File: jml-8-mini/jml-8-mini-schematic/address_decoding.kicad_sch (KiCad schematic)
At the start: 3 parts, among them U6 74LS04, U8 74LS139, U9 74LS32

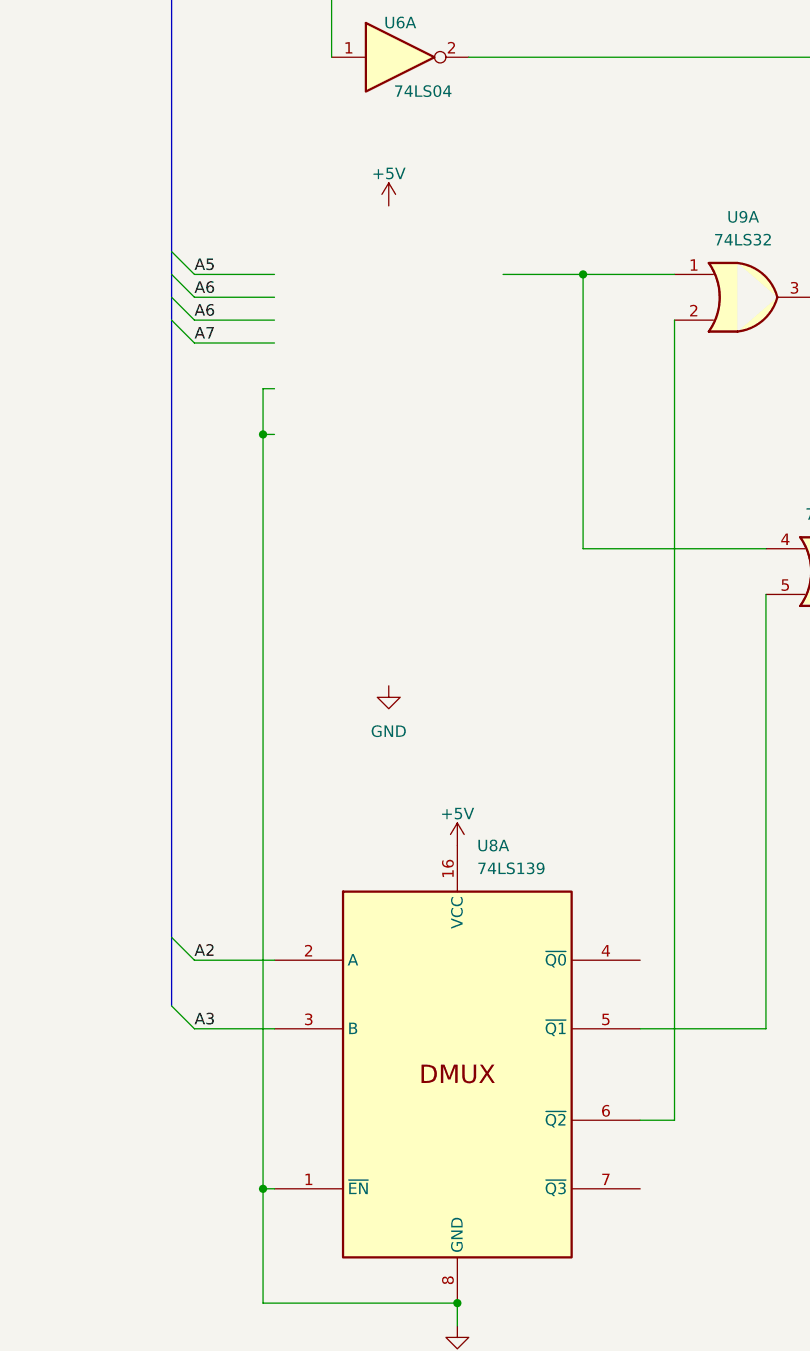
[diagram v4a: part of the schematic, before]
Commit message: lots of changes to schematic, redone to make easier to read and add to
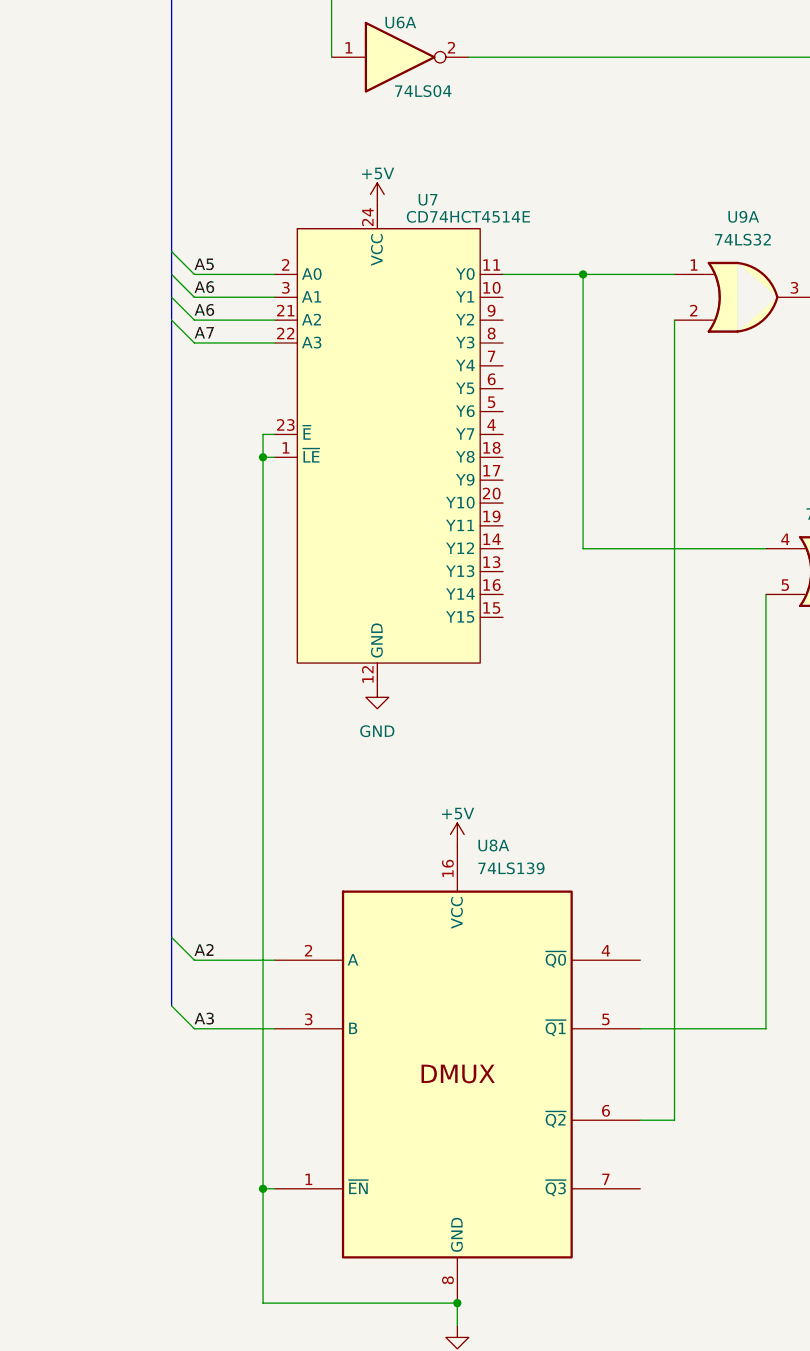
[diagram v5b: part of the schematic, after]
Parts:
- added U7: CD74HCT4514E, symbol jml-8-mini-library:CD74HCT4514E
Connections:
- net +5V: now also U7.24 (VCC)
- net A5: now also U7.2 (A0)
- net A6: now also U7.21 (A2), U7.3 (A1)
- net A7: now also U7.22 (A3)
- net GND: now also U7.1 (~{LE}), U7.12 (GND), U7.23 (~{E})
- net at U9.1, U9.4: now also U7.11 (Y0)
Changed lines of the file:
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@@
   (junction (at 85.09 185.42) (diameter 0) (color 0 0 0 0)
   )
+  (junction (at 63.5 91.44) (diameter 0) (color 0 0 0 0)
+  )
   (junction (at 63.5 172.72) (diameter 0) (color 0 0 0 0)
   )
-  (junction (at 63.5 88.9) (diameter 0) (color 0 0 0 0)
-  )
   (junction (at 53.34 29.21) (diameter 0) (color 0 0 0 0)
   )
@@
     (stroke (width 0) (type default))
   )
+  (wire (pts (xy 63.5 91.44) (xy 64.77 91.44))
+    (stroke (width 0) (type default))
+  )
   (bus (pts (xy 53.34 73.66) (xy 53.34 76.2))
     (stroke (width 0) (type default))
@@
     (stroke (width 0) (type default))
   )
-  (wire (pts (xy 63.5 88.9) (xy 63.5 172.72))
+  (wire (pts (xy 63.5 88.9) (xy 63.5 91.44))
     (stroke (width 0) (type default))
   )
@@
     (stroke (width 0) (type default))
   )
-  (wire (pts (xy 64.77 83.82) (xy 63.5 83.82))
-    (stroke (width 0) (type default))
-  )
   (wire (pts (xy 134.62 104.14) (xy 143.51 104.14))
     (stroke (width 0) (type default))
@@
     (stroke (width 0) (type default))
   )
-  (wire (pts (xy 63.5 83.82) (xy 63.5 88.9))
-    (stroke (width 0) (type default))
-  )
   (wire (pts (xy 55.88 154.94) (xy 64.77 154.94))
     (stroke (width 0) (type default))
@@
   )
   (wire (pts (xy 109.22 76.2) (xy 109.22 165.1))
+    (stroke (width 0) (type default))
+  )
+  (wire (pts (xy 63.5 91.44) (xy 63.5 172.72))
     (stroke (width 0) (type default))
   )
@@
         )
         (path "/7f93abb4-2372-4a9e-a664-5edb67349db4/0d9b5471-55ed-4c8b-801f-ea410459ca65"
-          (reference "#PWR?") (unit 1)
+          (reference "#PWR014") (unit 1)
         )
       )
@@
     )
   )
-  (symbol (lib_id "power:+5V") (at 77.47 63.5 0) (unit 1)
-    (in_bom yes) (on_board yes) (dnp no) (fields_autoplaced)
-    (property "Reference" "#PWR?" (at 77.47 67.31 0)
-      (effects (font (size 1.27 1.27)) hide)
-    )
-    (property "Value" "+5V" (at 77.47 59.944 0)
-      (effects (font (size 1.27 1.27)))
-    )
-    (property "Footprint" "" (at 77.47 63.5 0)
-      (effects (font (size 1.27 1.27)) hide)
-    )
-    (property "Datasheet" "" (at 77.47 63.5 0)
-      (effects (font (size 1.27 1.27)) hide)
-    )
-    (pin "1")
-    (instances
-      (project "jml-8-mini"
-        (path "/7f93abb4-2372-4a9e-a664-5edb67349db4/0d9b5471-55ed-4c8b-801f-ea410459ca65"
-          (reference "#PWR?") (unit 1)
+  (symbol (lib_id "power:+5V") (at 76.2 63.5 0) (unit 1)
+    (in_bom yes) (on_board yes) (dnp no) (fields_autoplaced)
+    (property "Reference" "#PWR06" (at 76.2 67.31 0)
+      (effects (font (size 1.27 1.27)) hide)
+    )
+    (property "Value" "+5V" (at 76.2 59.944 0)
+      (effects (font (size 1.27 1.27)))
+    )
+    (property "Footprint" "" (at 76.2 63.5 0)
+      (effects (font (size 1.27 1.27)) hide)
+    )
+    (property "Datasheet" "" (at 76.2 63.5 0)
+      (effects (font (size 1.27 1.27)) hide)
+    )
+    (pin "1")
+    (instances
+      (project "jml-8-mini"
+        (path "/7f93abb4-2372-4a9e-a664-5edb67349db4/0d9b5471-55ed-4c8b-801f-ea410459ca65"
+          (reference "#PWR06") (unit 1)
         )
       )
@@
     )
   )
-  (symbol (lib_id "power:GND") (at 77.47 116.84 0) (unit 1)
-    (in_bom yes) (on_board yes) (dnp no) (fields_autoplaced)
-    (property "Reference" "#PWR019" (at 77.47 123.19 0)
-      (effects (font (size 1.27 1.27)) hide)
-    )
-    (property "Value" "GND" (at 77.47 121.92 0)
-      (effects (font (size 1.27 1.27)))
-    )
-    (property "Footprint" "" (at 77.47 116.84 0)
-      (effects (font (size 1.27 1.27)) hide)
-    )
-    (property "Datasheet" "" (at 77.47 116.84 0)
+  (symbol (lib_id "jml-8-mini-library:CD74HCT4514E") (at 77.47 90.17 0) (unit 1)
+    (in_bom yes) (on_board yes) (dnp no)
+    (property "Reference" "U7" (at 80.645 62.865 0)
+      (effects (font (size 1.27 1.27)) (justify left))
+    )
+    (property "Value" "CD74HCT4514E" (at 79.375 64.77 0)
+      (effects (font (size 1.27 1.27)) (justify left))
+    )
+    (property "Footprint" "" (at 21.59 85.09 0)
+      (effects (font (size 1.27 1.27)) hide)
+    )
+    (property "Datasheet" "" (at 21.59 85.09 0)
+      (effects (font (size 1.27 1.27)) hide)
+    )
+    (pin "1")
+    (pin "10")
+    (pin "11")
+    (pin "12")
+    (pin "13")
+    (pin "14")
+    (pin "15")
+    (pin "16")
+    (pin "17")
+    (pin "18")
+    (pin "19")
+    (pin "2")
+    (pin "20")
+    (pin "21")
+    (pin "22")
+    (pin "23")
+    (pin "24")
+    (pin "3")
+    (pin "4")
+    (pin "5")
+    (pin "6")
+    (pin "7")
+    (pin "8")
+    (pin "9")
+    (instances
+      (project "jml-8-mini"
+        (path "/7f93abb4-2372-4a9e-a664-5edb67349db4/0d9b5471-55ed-4c8b-801f-ea410459ca65"
+          (reference "U7") (unit 1)
+        )
+      )
+    )
+  )
+  (symbol (lib_id "power:GND") (at 76.2 116.84 0) (unit 1)
+    (in_bom yes) (on_board yes) (dnp no) (fields_autoplaced)
+    (property "Reference" "#PWR019" (at 76.2 123.19 0)
+      (effects (font (size 1.27 1.27)) hide)
+    )
+    (property "Value" "GND" (at 76.2 121.92 0)
+      (effects (font (size 1.27 1.27)))
+    )
+    (property "Footprint" "" (at 76.2 116.84 0)
+      (effects (font (size 1.27 1.27)) hide)
+    )
+    (property "Datasheet" "" (at 76.2 116.84 0)
       (effects (font (size 1.27 1.27)) hide)
     )
@@
   (symbol (lib_id "power:+5V") (at 85.09 134.62 0) (unit 1)
     (in_bom yes) (on_board yes) (dnp no) (fields_autoplaced)
-    (property "Reference" "#PWR?" (at 85.09 138.43 0)
+    (property "Reference" "#PWR013" (at 85.09 138.43 0)
       (effects (font (size 1.27 1.27)) hide)
     )
@@
       (project "jml-8-mini"
         (path "/7f93abb4-2372-4a9e-a664-5edb67349db4/0d9b5471-55ed-4c8b-801f-ea410459ca65"
-          (reference "#PWR?") (unit 1)
-        )
-      )
+          (reference "#PWR013") (unit 1)
+        )
+      )

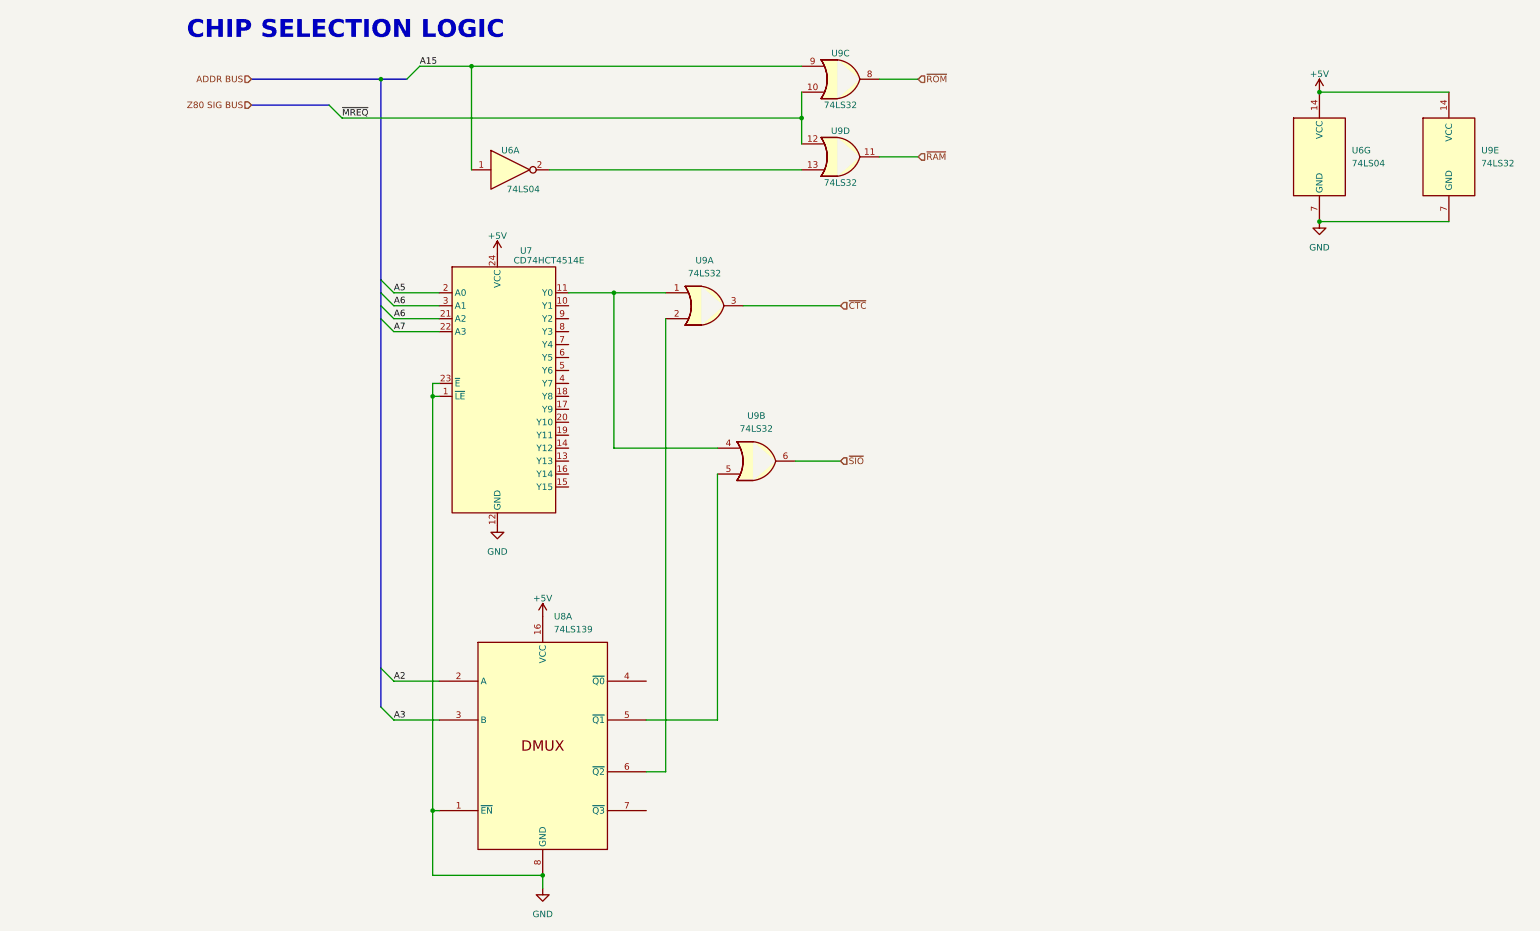
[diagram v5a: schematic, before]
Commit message: complete schematic
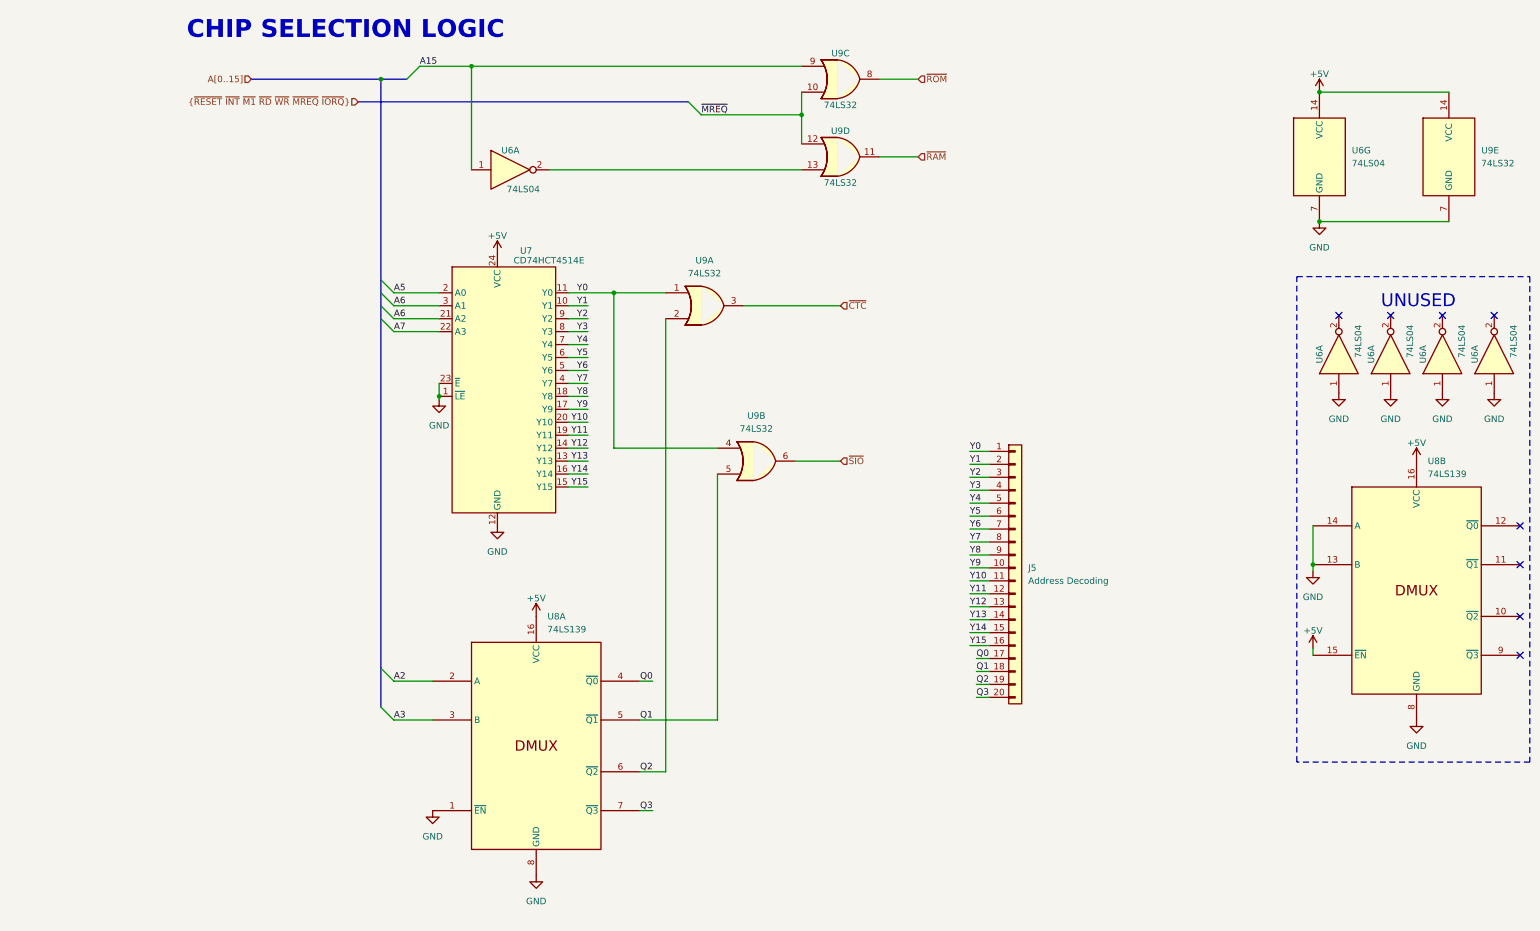
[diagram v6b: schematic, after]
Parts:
- added J5: Address Decoding, Connector_PinHeader_2.54mm:PinHeader_1x20_P2.54mm_Vertical, symbol Connector_Generic:Conn_01x20
- added U6 (x4): 74LS04, Package_DIP:DIP-14_W7.62mm_LongPads, symbol 74xx:74LS04
- added unit 2 of U8
- U6, U9: footprint (none) -> Package_DIP:DIP-14_W7.62mm_LongPads
- U7: footprint (none) -> Package_DIP:DIP-24_W15.24mm_LongPads
- U8: footprint (none) -> Package_DIP:DIP-16_W7.62mm_LongPads
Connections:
- net +5V: now also U8.15 (~{EN}), U8.16 (VCC)
- net GND: now also U6.1, U6.1, U6.1, U6.1, U8.13 (B), U8.14 (A), U8.8 (GND)
- net Y0: now reaches U7.11 (Y0), U9.1, U9.4
- net Y0: now also J5.1 (Pin_1)
- net Q2: now reaches U8.6 (~{Q2}), U9.2
- net Q2: now also J5.19 (Pin_19)
- net Q1: now reaches U8.5 (~{Q1}), U9.5
- net Q1: now also J5.18 (Pin_18)
- net Y1: now reaches U7.10 (Y1)
- net Y1: now also J5.2 (Pin_2)
- net Y13: now reaches U7.13 (Y13)
- net Y13: now also J5.14 (Pin_14)
- net Y12: now reaches U7.14 (Y12)
- net Y12: now also J5.13 (Pin_13)
- net Y15: now reaches U7.15 (Y15)
- net Y15: now also J5.16 (Pin_16)
- net Y14: now reaches U7.16 (Y14)
- net Y14: now also J5.15 (Pin_15)
- net Y9: now reaches U7.17 (Y9)
- net Y9: now also J5.10 (Pin_10)
- net Y8: now reaches U7.18 (Y8)
- net Y8: now also J5.9 (Pin_9)
- net Y11: now reaches U7.19 (Y11)
- net Y11: now also J5.12 (Pin_12)
- net Y10: now reaches U7.20 (Y10)
- net Y10: now also J5.11 (Pin_11)
- net Y7: now reaches U7.4 (Y7)
- net Y7: now also J5.8 (Pin_8)
- net Y6: now reaches U7.5 (Y6)
- net Y6: now also J5.7 (Pin_7)
- net Y5: now reaches U7.6 (Y5)
- net Y5: now also J5.6 (Pin_6)
- net Y4: now reaches U7.7 (Y4)
- net Y4: now also J5.5 (Pin_5)
- net Y3: now reaches U7.8 (Y3)
- net Y3: now also J5.4 (Pin_4)
- net Y2: now reaches U7.9 (Y2)
- net Y2: now also J5.3 (Pin_3)
- net Q0: now reaches U8.4 (~{Q0})
- net Q0: now also J5.17 (Pin_17)
- net Q3: now reaches U8.7 (~{Q3})
- net Q3: now also J5.20 (Pin_20)
- no-connect marks 0 -> 8
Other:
- note added: "UNUSED"
- moved on the sheet: U8A

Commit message: add to info section of schematic
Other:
- company: (none) -> https://github.com/jac-oblong/jml
- title: (none) -> JML-8 Mini Schematic
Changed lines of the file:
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@@
   (paper "A4")
   (title_block
+    (title "JML-8 Mini Schematic")
     (date "2023-10-02")
     (rev "A")
-    (comment 1 "Author: Jacob Long")
+    (company "https://github.com/jac-oblong/jml")
+    (comment 1 "Design of Z80 based microcomputer")
+    (comment 3 "Released under MIT License")
+    (comment 4 "Created by: Jacob Long (https://github.com/jac-oblong)")
   )
   (junction (at 237.49 57.15) (diameter 0) (color 0 0 0 0)

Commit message: update info section of schematic
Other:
- company: https://github.com/jac-oblong/jml -> https://github.com/jac-oblong/JML
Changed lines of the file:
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@@
     (date "2023-10-02")
     (rev "A")
-    (company "https://github.com/jac-oblong/jml")
+    (company "https://github.com/jac-oblong/JML")
     (comment 1 "Design of Z80 based microcomputer")
     (comment 3 "Released under MIT License")
